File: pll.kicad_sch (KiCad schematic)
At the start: 63 parts, among them CN11 UE75-A20-6000T, CN12 U77-A1114-30L1, CN15 731385033, Q6 DMN62D0U-7, T4 TC2-72T+, U11 SY75576LKY, U15 SN74LVC1G02DCK, U3 TI TPS79301DBV

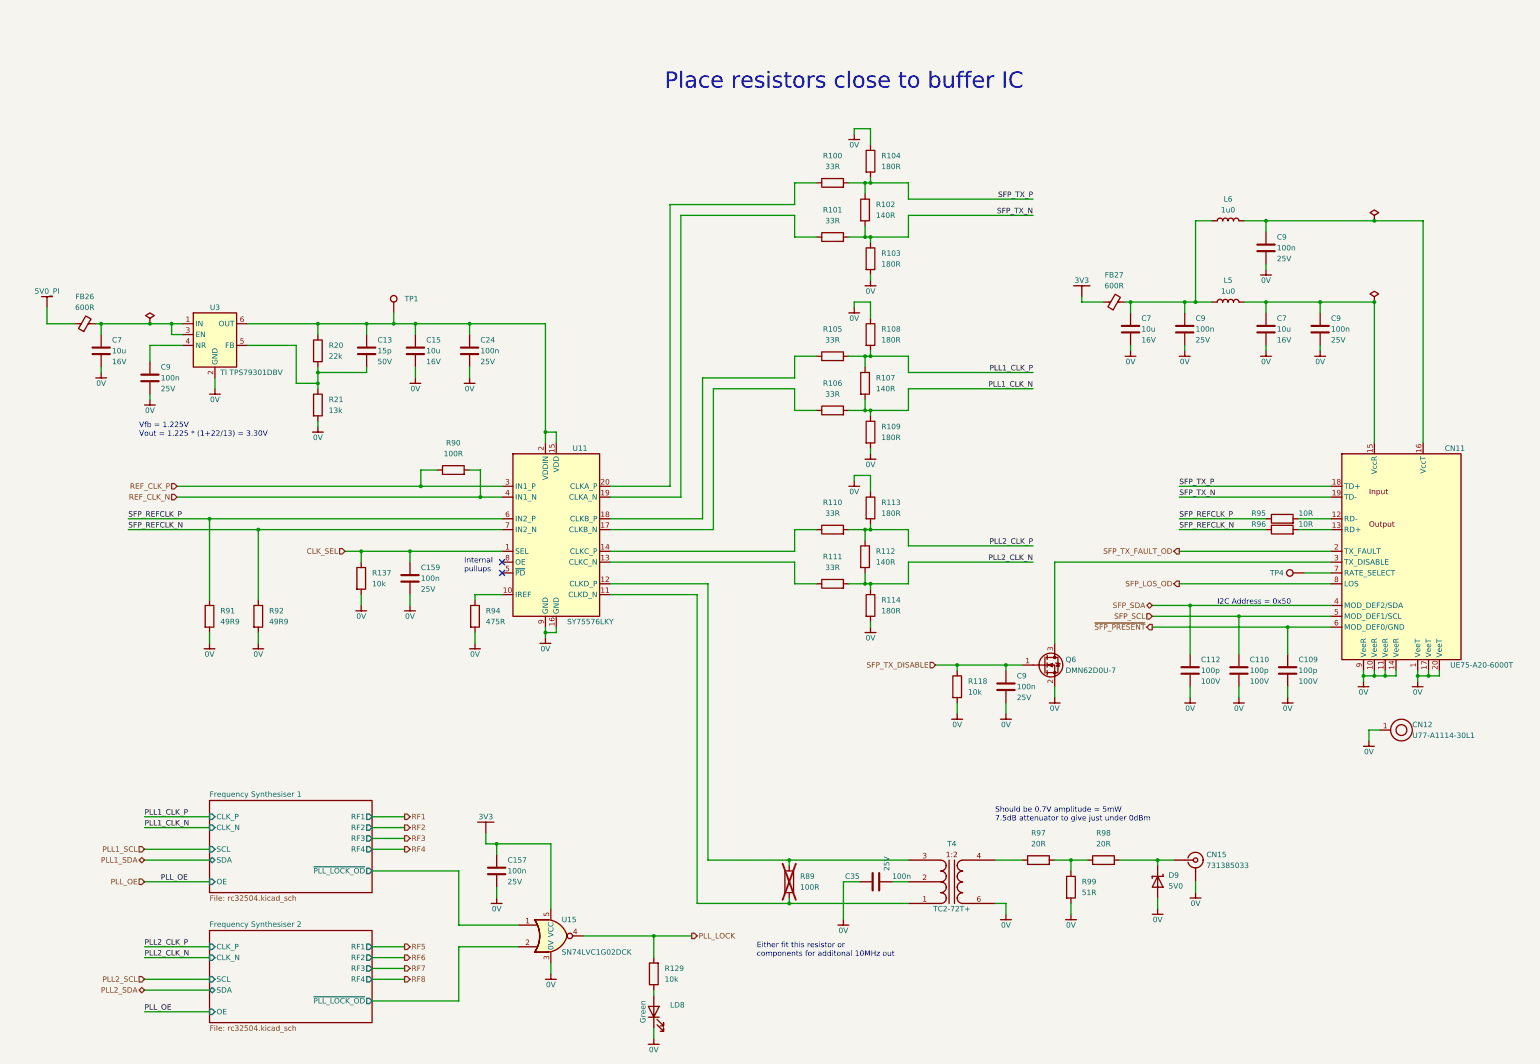
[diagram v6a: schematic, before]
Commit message: moving to discrete GPS recevier
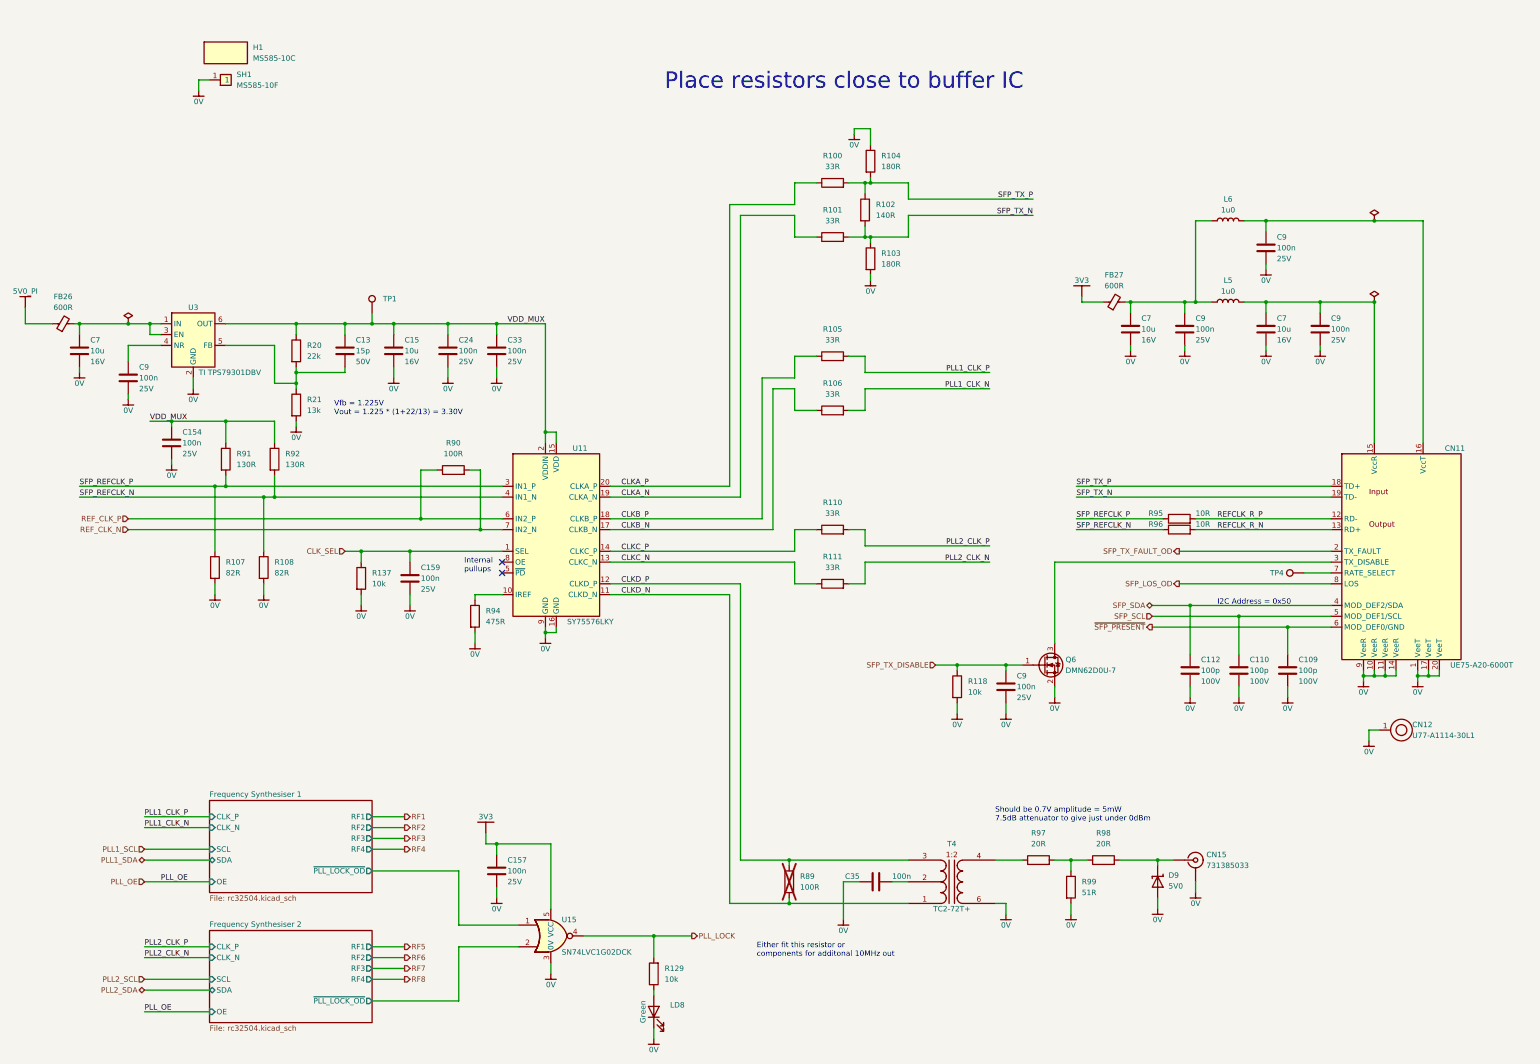
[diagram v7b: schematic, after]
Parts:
- removed R107, R112: 140R, Resistor_SMD:R_0402_1005Metric, symbol Auto_Library_WUT:KOA Speer RK73H1ETTP1400F
- removed R108, R109, R113, R114: 180R, Resistor_SMD:R_0402_1005Metric, symbol Auto_Library_WUT:KOA Speer RK73H1ETTP1800F
- removed R91, R92: 49R9, Resistor_SMD:R_0402_1005Metric, symbol Auto_Library_WUT:KOA Speer RK73H1ETTP49R9F
- added C154, C33: 100n, Capacitor_SMD:C_0402_1005Metric, symbol Preferred_WUT:Yageo CC0402KRX7R8BB104
- added H1: MS585-10C, symbol Shield_WUT:Masach_MS585-10C
- added R107, R108: 82R, Resistor_SMD:R_0402_1005Metric, symbol Auto_Library_WUT:KOA Speer RK73H1ETTP82R0F
- added R91, R92: 130R, Resistor_SMD:R_0402_1005Metric, symbol Auto_Library_WUT:KOA Speer RK73H1ETTP1300F
- added SH1: MS585-10F, Shield_WUT:Shield_Masach_MS585-10_58.2x49.4x4.7mm_SMD, symbol Shield_WUT:Masach_MS585-10F
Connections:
- net 0V: now also C154.2, C33.2, R107.2, R108.2, SH1.1
- net REF_CLK_N: now also U11.7 (IN2_N); no longer U11.4 (IN1_N)
- net REF_CLK_P: now also U11.6 (IN2_P); no longer U11.3 (IN1_P)
- net SFP_REFCLK_N: now also U11.4 (IN1_N), R108.1, R92.2; no longer U11.7 (IN2_N)
- net SFP_REFCLK_P: now also U11.3 (IN1_P), R107.1, R91.2; no longer U11.6 (IN2_P)
- net CLKC_P: now reaches R110.1, U11.14 (CLKC_P)
- net VDD_MUX: now reaches C13.1, C15.1, C24.1, R20.1, TP1.1, U11.15 (VDD), U11.2 (VDDIN), U3.6 (OUT)
- net VDD_MUX: now also C154.1, C33.1, R91.1, R92.1
- net REFCLK_R_P: now reaches CN11.12 (RD-), R95.2
- net CLKD_N: now reaches R89.2, T4.1, U11.11 (CLKD_N)
- net CLKD_P: now reaches R89.1, T4.3, U11.12 (CLKD_P)
- net CLKC_N: now reaches R111.1, U11.13 (CLKC_N)
- net CLKB_N: now reaches R106.1, U11.17 (CLKB_N)
- net CLKB_P: now reaches R105.1, U11.18 (CLKB_P)
- net CLKA_N: now reaches R101.1, U11.19 (CLKA_N)
- net CLKA_P: now reaches R100.1, U11.20 (CLKA_P)
- net REFCLK_R_N: now reaches CN11.13 (RD+), R96.2
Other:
- moved on the sheet: C13, C15, C24, C7, C9, FB26, R20, R21, R95, R96, TP1, U3
